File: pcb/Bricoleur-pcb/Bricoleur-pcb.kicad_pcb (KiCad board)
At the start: 2 copper layers, 1 part, among them U7 EFM32GG980

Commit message: Start of layout work + minor tweaks
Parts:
- added C1: 1U, Capacitor_SMD:C_0201_0603Metric, F.Cu at (138.8, 42.8)
- added C10: 100N, Capacitor_SMD:C_0402_1005Metric, F.Cu at (156.2, 30.2)
- added C11: 100N, Capacitor_SMD:C_0402_1005Metric, F.Cu at (97.8, 21.6)
- added C12: 100N, Capacitor_SMD:C_0402_1005Metric, F.Cu at (104.6, 25.4)
- added C13: 10U, Capacitor_SMD:C_0805_2012Metric, F.Cu at (144.8, 74.9)
- added C14: 1N, Capacitor_SMD:C_0402_1005Metric, F.Cu at (137.2, 21.6)
- added C15: 1N, Capacitor_SMD:C_0402_1005Metric, F.Cu at (142.2, 21.6)
- added C16: 1N, Capacitor_SMD:C_0402_1005Metric, F.Cu at (148.6, 21.6)
- added C2: 4U7, Capacitor_SMD:C_0805_2012Metric, F.Cu at (175.6, 29.2)
- added C3: 100N, Capacitor_SMD:C_0402_1005Metric, F.Cu at (121.9, 83.8)
- added C4: 1uF, Capacitor_SMD:C_0603_1608Metric, F.Cu at (144.5, 42.8)
- added C5: 10U, Capacitor_SMD:C_0805_2012Metric, F.Cu at (153.8, 38.6)
- added C6: 10N, Capacitor_SMD:C_0402_1005Metric, F.Cu at (152.0, 47.1)
- added C7: 10N, Capacitor_SMD:C_0402_1005Metric, F.Cu at (162.5, 33.5)
- added C8: 100N, Capacitor_SMD:C_0402_1005Metric, F.Cu at (149.5, 52.2)
- added C9: 100N, Capacitor_SMD:C_0402_1005Metric, F.Cu at (162.8, 41.9)
- added D1: LED, LED_SMD:LED_0201_0603Metric, F.Cu at (112.1, 16.5)
- added D2: LED, LED_SMD:LED_0201_0603Metric, F.Cu at (111.8, 20.3)
- added D3: LED, LED_SMD:LED_0201_0603Metric, F.Cu at (111.7, 25.4)
- added J1: USB_B_Micro, Connector_USB:USB_B_OST_USB-B1HSxx_Horizontal, F.Cu at (267.2, 21.6)
- added J2: Conn_02x10_Odd_Even, Connector_IDC:IDC-Header_2x10_P2.54mm_Vertical, F.Cu at (209.6, 21.6)
- added L1: 220R 2A CBF221HC, Bricoleur-custom:CBF221HC, F.Cu at (259.2, 16.5)
- added L2: CBF102WB, Bricoleur-custom:CBF102WB, F.Cu at (109.2, 47.0)
- added R1: 100R, Resistor_SMD:R_0402_1005Metric, F.Cu at (115.6, 90.2)
- added R10: 3K, Capacitor_SMD:C_0402_1005Metric, F.Cu at (115.6, 25.4)
- added R11: 100R, Resistor_SMD:R_0402_1005Metric, F.Cu at (163.8, 85.1)
- added R12: 100R, Resistor_SMD:R_0402_1005Metric, F.Cu at (175.3, 85.1)
- added R13: 100R, Resistor_SMD:R_0402_1005Metric, F.Cu at (189.2, 86.4)
- added R14: 100K, Resistor_SMD:R_0402_1005Metric, F.Cu at (200.7, 48.3)
- added R15: 100K, Resistor_SMD:R_0402_1005Metric, F.Cu at (200.7, 44.5)
- added R16: 10K, Resistor_SMD:R_0402_1005Metric, F.Cu at (129.0, 37.5)
- added R17: 100K, Resistor_SMD:R_0402_1005Metric, F.Cu at (131.0, 29.3)
- added R2: 15R, Resistor_SMD:R_0402_1005Metric, F.Cu at (260.4, 24.1)
- added R3: 15R, Resistor_SMD:R_0402_1005Metric, F.Cu at (260.4, 27.9)
- added R4: 1R, Resistor_SMD:R_0402_1005Metric, F.Cu at (157.3, 45.1)
- added R5: 1M, Resistor_SMD:R_0402_1005Metric, F.Cu at (137.2, 16.7)
- added R6: 1M, Resistor_SMD:R_0402_1005Metric, F.Cu at (142.2, 16.5)
- added R7: 1M, Resistor_SMD:R_0402_1005Metric, F.Cu at (147.3, 16.5)
- added R8: 3K, Resistor_SMD:R_0402_1005Metric, F.Cu at (116.1, 16.5)
- added R9: 3K, Capacitor_SMD:C_0402_1005Metric, F.Cu at (116.1, 20.3)
- added SW2: SW_Push, Bricoleur-custom:SWITCH_WURTH_4301182043816, F.Cu at (111.8, 83.8)
- added SW3: SW_Push, Bricoleur-custom:SWITCH_WURTH_4301182043816, F.Cu at (159.3, 76.8)
- added SW4: SW_Push, Bricoleur-custom:SWITCH_WURTH_4301182043816, F.Cu at (171.4, 76.2)
- added SW5: SW_Push, Bricoleur-custom:SWITCH_WURTH_4301182043816, F.Cu at (184.2, 76.2)
- added U1: Ultrasonic-LV-EZ0, Connector_IDC:IDC-Header_2x03_P2.54mm_Vertical, F.Cu at (245.1, 63.5)
- added U10: VESD05A8A-HNH, Bricoleur-custom:VESD05A8A-HNH, F.Cu at (137.2, 28.5)
- added U11: SW_DP3T, Bricoleur-custom:SW_CK_JS203011, F.Cu at (268.0, 88.9)
- added U2: PYNQ-Shield-Bricoleur-pcb-cache, Bricoleur-custom:PYNQ_Shield, F.Cu at (248.9, 123.3)
- added U3: Ultrasonic-LV-EZ0, Connector_IDC:IDC-Header_2x03_P2.54mm_Vertical, F.Cu at (265.4, 63.5)
- added U4: Ultrasonic-LV-EZ0, Connector_IDC:IDC-Header_2x03_P2.54mm_Vertical, F.Cu at (255.3, 63.5)
- added U5: Arducam-OV5642, Connector_IDC:IDC-Header_2x10_P2.54mm_Vertical, F.Cu at (235.3, 107.3)
- added U6: Arducam-OV5642, Connector_IDC:IDC-Header_2x10_P2.54mm_Vertical, F.Cu at (253.1, 134.0)
- added U8: UART_BOOT, Connector_PinHeader_2.54mm:PinHeader_1x03_P2.54mm_Vertical, F.Cu at (228.6, 55.9)
- added U9: IP4220CZ6, Bricoleur-custom:IP4220CZ6, F.Cu at (269.0, 41.8)
- U7: value EFM32GG980 -> QFP100_14X14
- moved U7 49.4 mm to (236.2, 35.4)
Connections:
- net Net-(U7-Pad32) renamed /VSS07
- U7 pad 10: Net-(U7-Pad10) -> DEBUG_EXT_CABLE_ATTACH
- U7 pad 16: Net-(U7-Pad16) -> GND
- U7 pad 17: Net-(U7-Pad17) -> DH_VTARGET
- U7 pad 31: Net-(U7-Pad31) -> DH_VTARGET
- U7 pad 36: Net-(U7-Pad36) -> DH_#RESET
- U7 pad 37: Net-(U7-Pad37) -> DBG_PB_1
- U7 pad 38: Net-(U7-Pad38) -> DBG_PB_2
- U7 pad 39: Net-(U7-Pad39) -> DBG_PB_3
- U7 pad 41: Net-(U7-Pad41) -> /AVDDU7
- U7 pad 44: Net-(U7-Pad44) -> DH_VTARGET
- U7 pad 45: Net-(U7-Pad45) -> /AVDDU7
- U7 pad 57: Net-(U7-Pad57) -> DH_VTARGET
- U7 pad 58: Net-(U7-Pad58) -> GND
- U7 pad 62: Net-(U7-Pad62) -> DBG_LED_1
- U7 pad 63: Net-(U7-Pad63) -> DBG_LED_2
- U7 pad 64: Net-(U7-Pad64) -> DBG_LED_3
- U7 pad 68: Net-(U7-Pad68) -> /US0_CS
- U7 pad 69: Net-(U7-Pad69) -> /US0_CLK
- U7 pad 70: Net-(U7-Pad70) -> /US0_RX
- U7 pad 71: Net-(U7-Pad71) -> /US0_TX
- U7 pad 72: Net-(U7-Pad72) -> Net-(C2-Pad2)
- U7 pad 76: Net-(U7-Pad76) -> DH_TCK_SWCLK
- U7 pad 77: Net-(U7-Pad77) -> DH_TMS_SWDIO
- U7 pad 78: Net-(U7-Pad78) -> DH_TDO_SWO
- U7 pad 79: Net-(U7-Pad79) -> Net-(C2-Pad2)
- U7 pad 8: Net-(U7-Pad8) -> DH_VTARGET
- U7 pad 82: Net-(U7-Pad82) -> DH_VTARGET
- U7 pad 83: Net-(U7-Pad83) -> GND

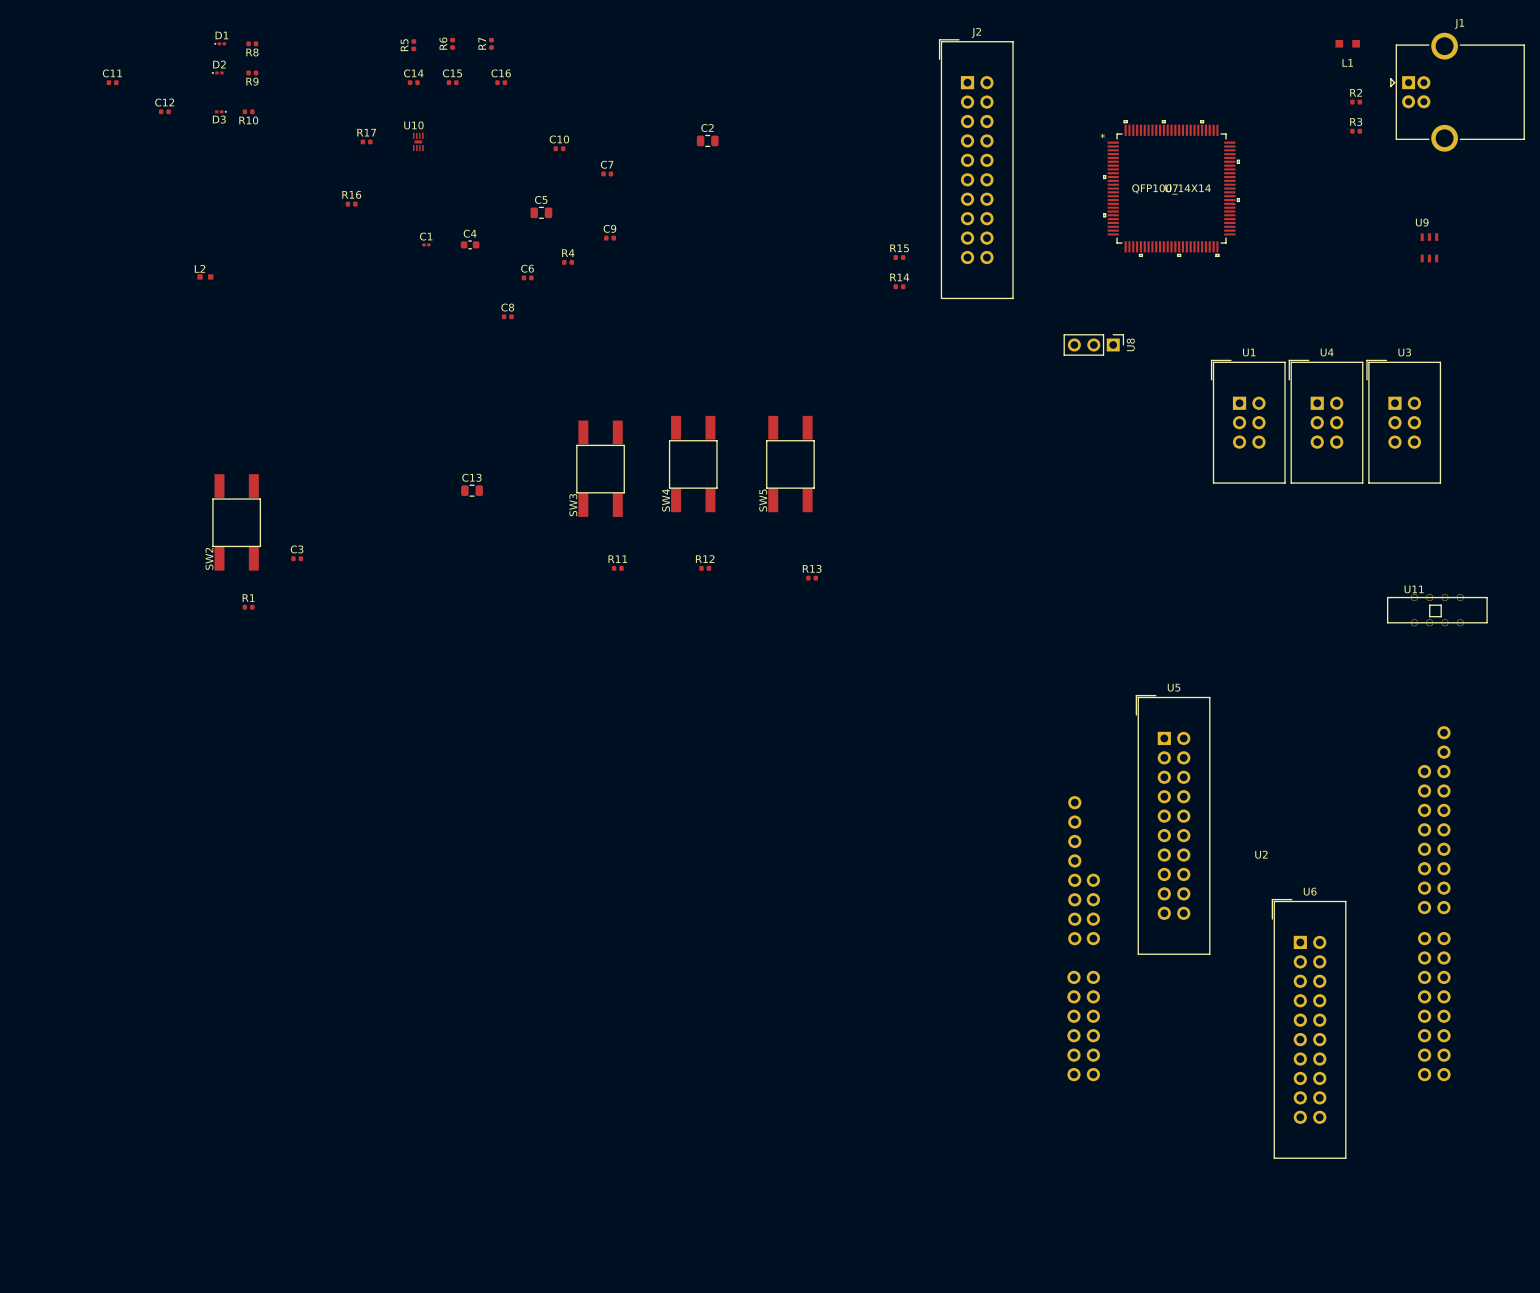
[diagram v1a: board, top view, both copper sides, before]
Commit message: Finished camera connection, started on MC. Changed debug protection diodes sharing pattern to match debug connector.
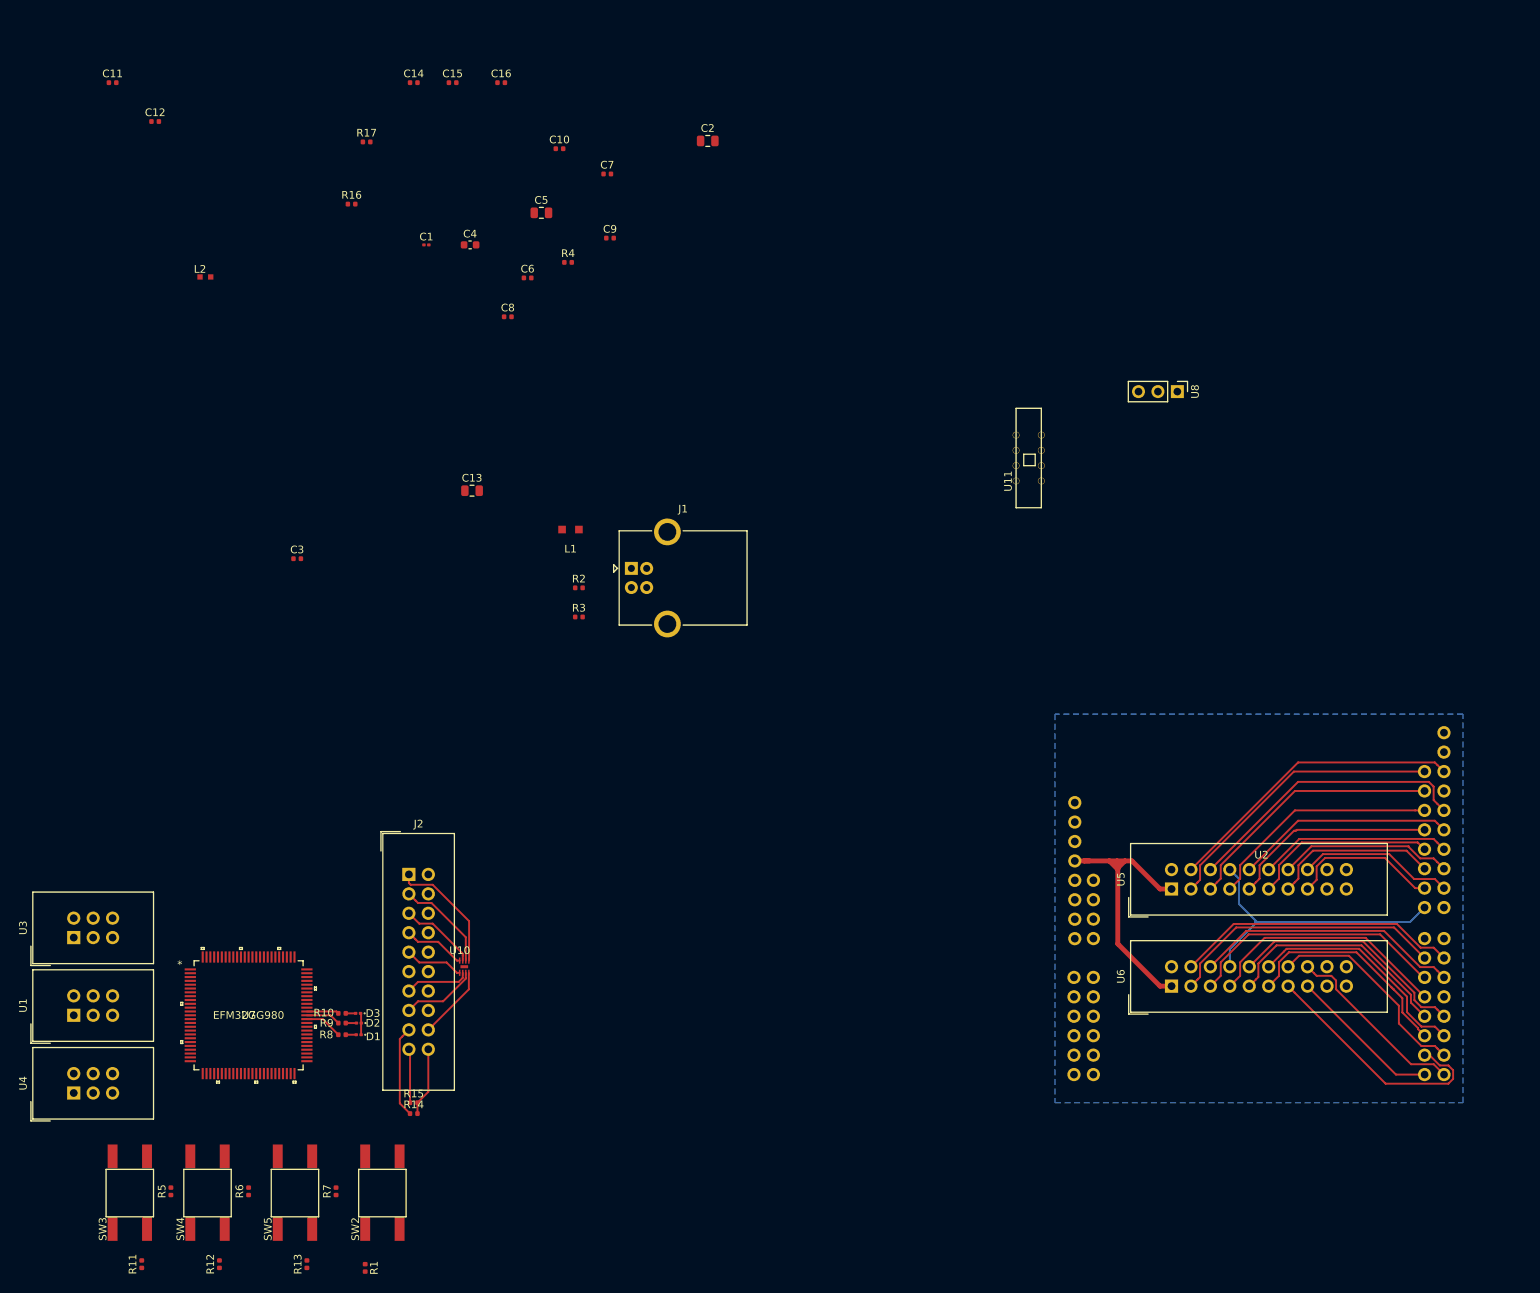
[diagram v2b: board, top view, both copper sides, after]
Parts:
- removed U9: IP4220CZ6, Bricoleur-custom:IP4220CZ6
- U7: value QFP100_14X14 -> EFM32GG980
- moved U3 186.3 mm to (92.7, 133.3), turned to 90 degrees
- moved U4 185.9 mm to (92.7, 153.7), turned to 90 degrees
- moved U1 172.1 mm to (92.7, 143.5), turned to 90 degrees
- moved U7 162.0 mm to (115.6, 143.5)
- moved R5 153.2 mm to (105.4, 166.5)
- moved R6 152.4 mm to (115.6, 166.5)
- moved R7 151.4 mm to (127.0, 166.5)
- moved D1 130.8 mm to (130.0, 146.1), turned to 180 degrees
- moved R8 130.1 mm to (127.8, 146.1), turned to 0 degrees
- moved R15 127.4 mm to (137.2, 154.9)
- moved J2 126.7 mm to (136.5, 125.1)
- moved D2 125.5 mm to (130.0, 144.5), turned to 180 degrees
- moved R14 125.4 mm to (137.2, 156.4)
- moved R9 124.8 mm to (127.8, 144.5), turned to 0 degrees
- moved J1 119.8 mm to (165.6, 85.1)
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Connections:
- net Net-(U1-Pad2) renamed PULSE
- D1 pad 2: GND -> Net-(D1-Pad2)
- D2 pad 2: GND -> Net-(D2-Pad2)
- D3 pad 2: GND -> Net-(D3-Pad2)
- J1 pad 4: Net-(J1-Pad4) -> (no net)
- J2 pad 2: Net-(J2-Pad2) -> (no net)
- R10 pad 2: GND -> Net-(D3-Pad2)
- R8 pad 2: GND -> Net-(D1-Pad2)
- R9 pad 2: GND -> Net-(D2-Pad2)
- U1 pad 1: Net-(U1-Pad1) -> (no net)
- U1 pad 3: Net-(U1-Pad3) -> (no net)
- U1 pad 5: Net-(U1-Pad5) -> (no net)
- U10 pad 1: DEBUG_EXT_CABLE_ATTACH -> DH_TMS_SWDIO
- U10 pad 2: DH_VTARGET -> DH_TDI
- U10 pad 4: DH_TDI -> DH_VTARGET
- U10 pad 5: DH_TMS_SWDIO -> DH_TCK_SWCLK
- U10 pad 6: DH_TCK_SWCLK -> DH_TDO_SWO
- U10 pad 7: DH_TDO_SWO -> DH_#RESET
- U10 pad 8: DH_#RESET -> DEBUG_EXT_CABLE_ATTACH
- U11 pad 4: /DBG_Supply -> (no net)
- U2 pad 1: Net-(U2-Pad1) -> (no net)
- U2 pad 10: Net-(U2-Pad10) -> (no net)
- U2 pad 11: Net-(U2-Pad11) -> (no net)
- U2 pad 12: Net-(U2-Pad12) -> (no net)
- U2 pad 13: Net-(U2-Pad13) -> (no net)
- U2 pad 14: Net-(U2-Pad14) -> (no net)
- U2 pad 15: Net-(U2-Pad15) -> (no net)
- U2 pad 16: Net-(U2-Pad16) -> (no net)
- U2 pad 17: Net-(U2-Pad17) -> (no net)
- U2 pad 18: Net-(U2-Pad18) -> (no net)
- U2 pad 19: Net-(U2-Pad19) -> (no net)
- U2 pad 2: Net-(U2-Pad2) -> (no net)
- U2 pad 20: Net-(U2-Pad20) -> (no net)
- U2 pad 21: Net-(U2-Pad21) -> (no net)
- U2 pad 22: Net-(U2-Pad22) -> (no net)
- U2 pad 23: Net-(U2-Pad23) -> (no net)
- U2 pad 24: Net-(U2-Pad24) -> (no net)
- U2 pad 25: Net-(U2-Pad25) -> (no net)
- U2 pad 26: Net-(U2-Pad26) -> (no net)
- U2 pad 28: Net-(U2-Pad28) -> (no net)
- U2 pad 3: Net-(U2-Pad3) -> (no net)
- U2 pad 5: /PYNQ_5V0 -> (no net)
- U2 pad 8: Net-(U2-Pad8) -> (no net)
- U2 pad 9: Net-(U2-Pad9) -> (no net)
- U3 pad 1: Net-(U3-Pad1) -> (no net)
- U3 pad 3: Net-(U3-Pad3) -> (no net)
- U3 pad 5: Net-(U3-Pad5) -> (no net)
- U4 pad 1: Net-(U4-Pad1) -> (no net)
- U4 pad 3: Net-(U4-Pad3) -> (no net)
- U4 pad 5: Net-(U4-Pad5) -> (no net)
- U5 pad 18: Net-(U5-Pad18) -> (no net)
- U5 pad 19: Net-(U5-Pad19) -> (no net)
- U6 pad 18: Net-(U6-Pad18) -> (no net)
- U6 pad 19: Net-(U6-Pad19) -> (no net)
- U7 pad 100: Net-(U7-Pad100) -> (no net)
- U7 pad 11: Net-(U7-Pad11) -> (no net)
- U7 pad 12: Net-(U7-Pad12) -> (no net)
- U7 pad 13: Net-(U7-Pad13) -> (no net)
- U7 pad 14: Net-(U7-Pad14) -> (no net)
- U7 pad 15: Net-(U7-Pad15) -> (no net)
- U7 pad 18: Net-(U7-Pad18) -> (no net)
- U7 pad 19: Net-(U7-Pad19) -> (no net)
- U7 pad 2: Net-(U7-Pad2) -> (no net)
- U7 pad 20: Net-(U7-Pad20) -> (no net)
- U7 pad 21: Net-(U7-Pad21) -> (no net)
- U7 pad 22: Net-(U7-Pad22) -> (no net)
- U7 pad 23: Net-(U7-Pad23) -> (no net)
- U7 pad 24: Net-(U7-Pad24) -> (no net)
- U7 pad 25: Net-(U7-Pad25) -> (no net)
- U7 pad 26: Net-(U7-Pad26) -> (no net)
- U7 pad 27: Net-(U7-Pad27) -> (no net)
- U7 pad 28: Net-(U7-Pad28) -> (no net)
- U7 pad 29: Net-(U7-Pad29) -> (no net)
- U7 pad 3: Net-(U7-Pad3) -> (no net)
- U7 pad 30: Net-(U7-Pad30) -> (no net)
- U7 pad 32: /VSS07 -> (no net)
- U7 pad 33: Net-(U7-Pad33) -> (no net)
- U7 pad 34: Net-(U7-Pad34) -> (no net)
- U7 pad 35: Net-(U7-Pad35) -> (no net)
- U7 pad 40: Net-(U7-Pad40) -> (no net)
- U7 pad 42: Net-(U7-Pad42) -> (no net)
- U7 pad 43: Net-(U7-Pad43) -> (no net)
- U7 pad 46: Net-(U7-Pad46) -> (no net)
- U7 pad 47: Net-(U7-Pad47) -> (no net)
- U7 pad 48: Net-(U7-Pad48) -> (no net)
- U7 pad 49: Net-(U7-Pad49) -> (no net)
- U7 pad 50: Net-(U7-Pad50) -> (no net)
- U7 pad 51: Net-(U7-Pad51) -> (no net)
- U7 pad 52: Net-(U7-Pad52) -> (no net)
- U7 pad 53: Net-(U7-Pad53) -> (no net)
- U7 pad 54: Net-(U7-Pad54) -> (no net)
- U7 pad 55: Net-(U7-Pad55) -> (no net)
- U7 pad 56: Net-(U7-Pad56) -> (no net)
- U7 pad 60: Net-(U7-Pad60) -> (no net)
- U7 pad 61: Net-(U7-Pad61) -> (no net)
- U7 pad 65: Net-(U7-Pad65) -> (no net)
- U7 pad 66: Net-(U7-Pad66) -> (no net)
- U7 pad 67: Net-(U7-Pad67) -> (no net)
- U7 pad 7: Net-(U7-Pad7) -> (no net)
- U7 pad 80: Net-(U7-Pad80) -> (no net)
- U7 pad 81: Net-(U7-Pad81) -> (no net)
- U7 pad 84: Net-(U7-Pad84) -> (no net)
- U7 pad 85: Net-(U7-Pad85) -> (no net)
- U7 pad 86: Net-(U7-Pad86) -> (no net)
- U7 pad 87: Net-(U7-Pad87) -> (no net)
- U7 pad 88: Net-(U7-Pad88) -> (no net)
- U7 pad 89: Net-(U7-Pad89) -> (no net)
- U7 pad 9: Net-(U7-Pad9) -> (no net)
- U7 pad 90: Net-(U7-Pad90) -> (no net)
- U7 pad 91: Net-(U7-Pad91) -> (no net)
- U7 pad 92: Net-(U7-Pad92) -> (no net)
- U7 pad 93: Net-(U7-Pad93) -> (no net)
- U7 pad 96: Net-(U7-Pad96) -> (no net)
- U7 pad 97: Net-(U7-Pad97) -> (no net)
- U7 pad 98: Net-(U7-Pad98) -> (no net)
- U7 pad 99: Net-(U7-Pad99) -> (no net)
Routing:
- net /CAM1_SDATA: track 0.00 -> 39.4 mm
- net /CAM_CLK: track 0.00 -> 38.8 mm
- net PYNQ_3V3: track 0.00 -> 38.1 mm
- net /CAM1_SCL: track 0.00 -> 38.0 mm
- net /CAM1_HREF: track 0.00 -> 37.9 mm
- net /CAM0_SDATA: track 0.00 -> 37.2 mm
- net /CAM0_SCL: track 0.00 -> 36.4 mm
- net /CAM0_HREF: track 0.00 -> 35.0 mm
- net /CAM1_VSYNC: track 0.00 -> 34.3 mm
- net /CAM0_VSYNC: track 0.00 -> 34.2 mm
- net /CAM0_DOUT5: track 0.00 -> 32.8 mm
- net /CAM0_PCLK: track 0.00 -> 32.3 mm
- net /CAM0_DOUT8: track 0.00 -> 31.5 mm
- net /CAM1_PCLK: track 0.00 -> 30.7 mm
- net /CAM0_DOUT9: track 0.00 -> 30.6 mm
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- added copper zone on B.Cu, net GND
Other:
- net class Default: clearance 0.2 -> 0.1; trace_width 0.25 -> 0.254
- net class Power added: clearance 0.1, trace_width 0.254, via_dia 0.8, via_drill 0.4
- rule trace_clearance: 0.2 -> 0.1
